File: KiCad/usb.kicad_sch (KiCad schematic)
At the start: 14 parts, among them J20 RJE361882415, J22 USB3_A_Stacked, J23 USB3_IDC, J24 Conn_02x05_Odd_Even, U28 H5VU25U, U29 H5VU25U, U30 H5VU25U, U31 H5VU25U, U32 H5VU25U, U33 H5VU25U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

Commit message: Re-annotate schematic
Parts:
- renumbered J20 to J19, J22 to J21, J23 to J22, J24 to J23

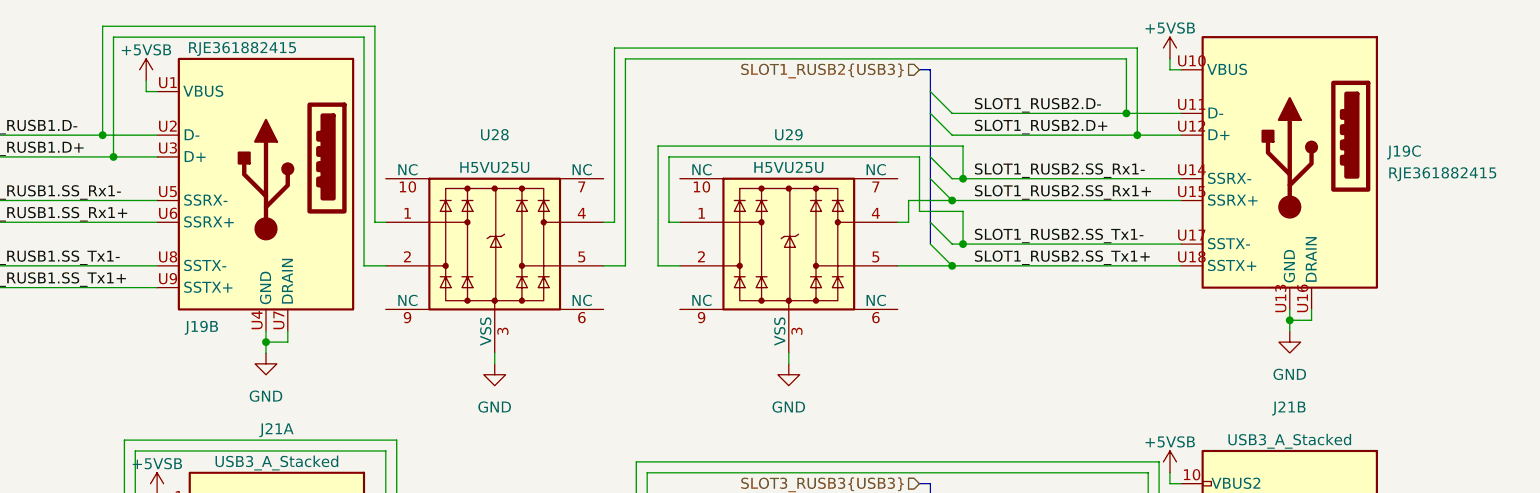
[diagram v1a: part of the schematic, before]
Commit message: Begin moving IO to module sheets
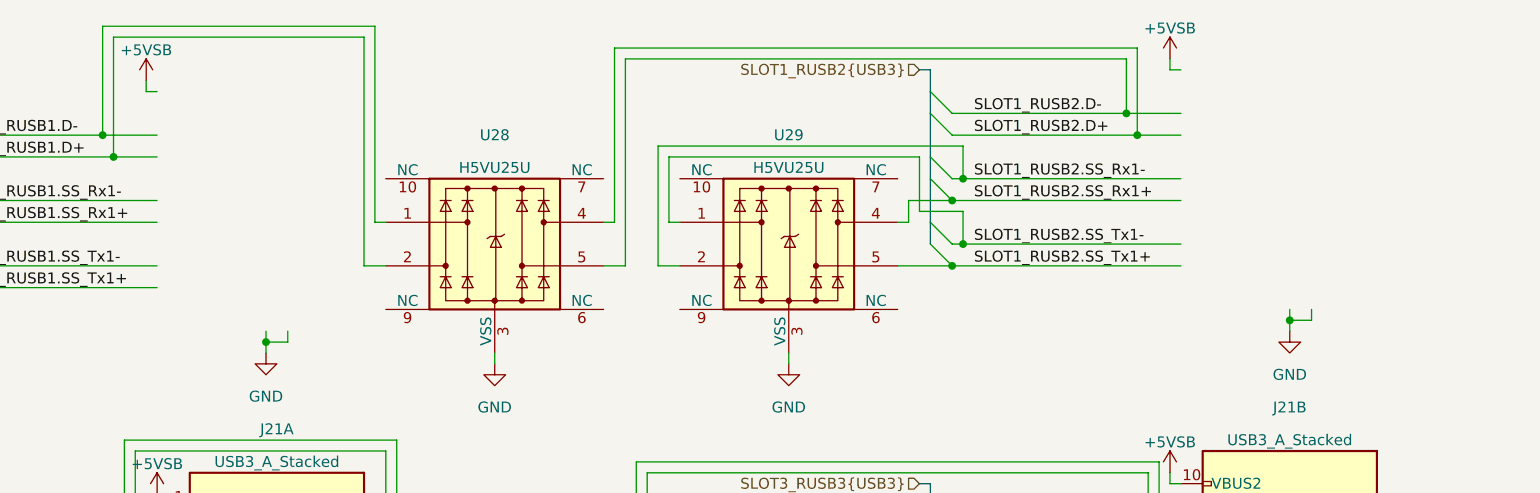
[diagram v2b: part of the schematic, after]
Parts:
- removed J19: RJE361882415, RJE361882145:AMPHENOL_RJE361882415, symbol Custom:1xRJ45+2xUSB3
